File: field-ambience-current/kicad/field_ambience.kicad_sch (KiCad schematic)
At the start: 0 parts

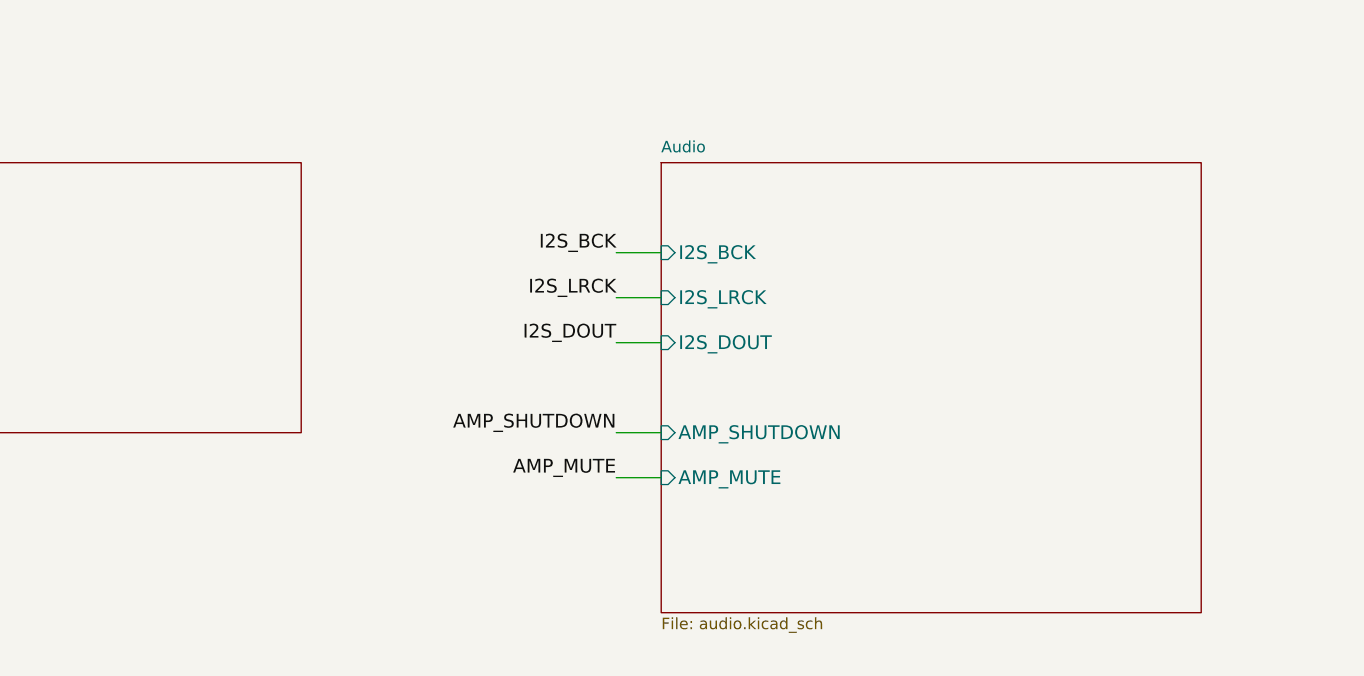
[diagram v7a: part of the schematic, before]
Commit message: v0.6.3-r5 N1-Fix: PCM5102A XSMT via MCP23017 GPA5 GPIO control
User-Wunsch: "lieber direkt haben als nicht haben" — explizite GPIO-
gesteuerte Pop-Suppression für PCM5102A statt nur statischem Pull-Up.

Hardware-Änderungen:

audio.kicad_sch (PCM5102A Pin 17 XSMT):
- BEFORE: R_XSMT 10k pull-up zu DVDD (chip statisch un-muted)
- AFTER:
  - R_XSMT_PD 10k pull-down zu GND (boot-safe default LOW = muted)
  - hier-input PCM_XSMT (vom MCP23017 via I²C-Steuerung)
  → Während Pico-Reset/Boot: XSMT bleibt LOW (DAC stumm), egal was
     der PCM5102A intern macht.

mcp.kicad_sch (MCP23017 GPA5 = Pin 26):
- BEFORE: NC_GPA5 reserve label (Pin ungenutzt)
- AFTER: hier-output PCM_XSMT (drives PCM5102A XSMT via PCM_XSMT net)

root.kicad_sch:
- MCP-Sheet-Box bekommt PCM_XSMT output pin (right side y=215)
- Audio-Sheet-Box bekommt PCM_XSMT input pin (left side y=240)
- Audio-Sheet-Box-Höhe von 50 → 55 erweitert (für zusätzlichen Pin)
- Cross-Sheet Label-Bridge PCM_XSMT zwischen MCP und Audio

Firmware-Sequenz (dokumentiert in SPEC v0.6.3-r5):
1. Boot: MCP23017-Pins default Input → R_XSMT_PD zieht XSMT LOW → PCM stumm
2. I²C-Init: MCP23017 GPA5 als Output, default 0 (XSMT bleibt LOW)
3. Power-Rails stabilisieren (~50 ms)
4. PAM8403 enable: GP28 (MUTE) HIGH, 100 ms später GP27 (SHDN) HIGH
5. PCM un-mute: MCP GPA5 HIGH → PCM_XSMT = +3V3 → DAC un-muted
6. → kein Pop am Speaker, kein DAC-Hochfahr-Knack

SPEC §7 MCP23017 Pin-Tabelle aktualisiert: GPA5 dokumentiert als
PCM_XSMT-Control, nicht mehr als reserve.

Analyzer-Status: 0 functional errors, 18 warnings (one less than r4 weil
NC_GPA5 label weg ist), 90 components (R_XSMT durch R_XSMT_PD ersetzt,
keine net-Change), 119 nets.

Verified via analyzer pin_nets:
- U3 Pin 17 (XSMT) → PCM_XSMT ✓
- U2 Pin 26 (GPA5) → PCM_XSMT ✓
- R_XSMT_PD pin1 = PCM_XSMT, pin2 = GND ✓

Damit ist Pop-Suppression jetzt belt-and-suspenders:
- Boot: PAM /MUTE LOW (R_MUTE_PD) + /SHDN LOW (R_SHDN_PD) + PCM XSMT LOW
- Operation: alle drei HIGH durch Firmware
- Shutd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
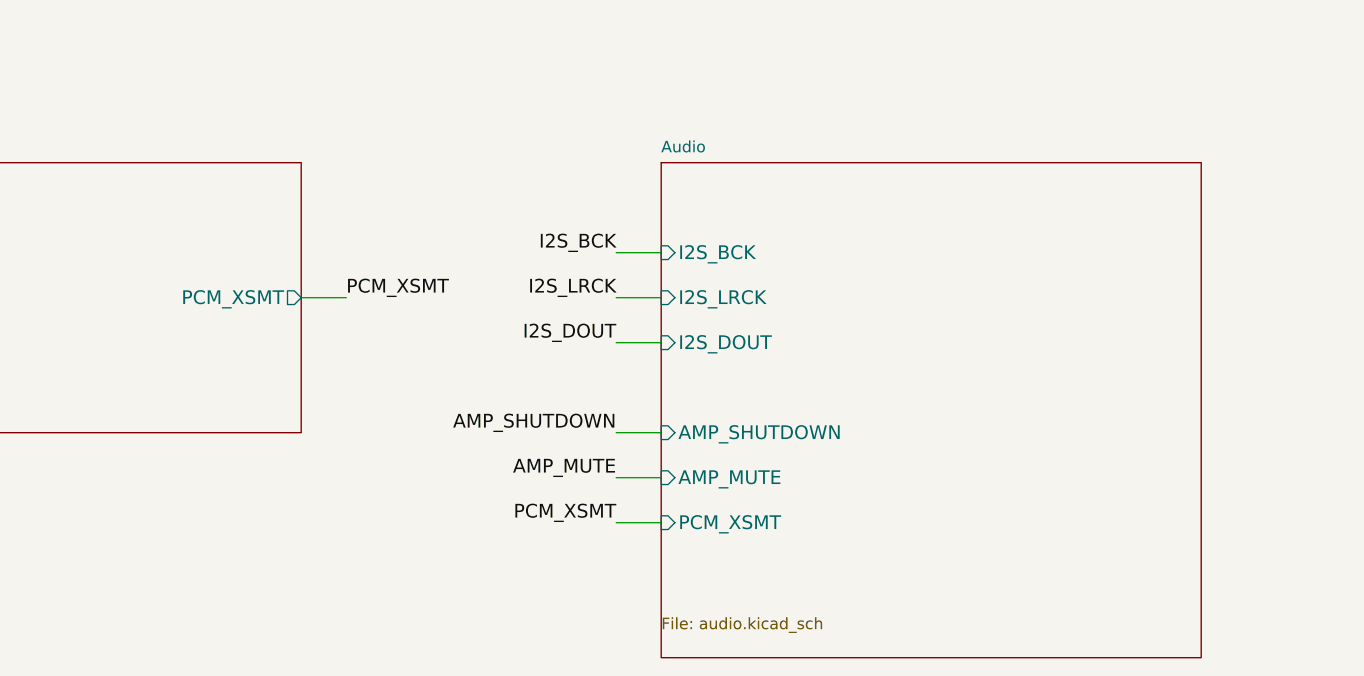
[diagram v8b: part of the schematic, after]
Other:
- sheet Audio ports: added PCM_XSMT; removed none
- sheet MCP23017 ports: added PCM_XSMT; removed none
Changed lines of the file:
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@@
     (pin "MCP_INT" output (at 130 220 180)
       (effects (font (size 1.524 1.524)) (justify left))
+)
+    (pin "PCM_XSMT" output (at 190 215 0)
+      (effects (font (size 1.524 1.524)) (justify right))
 ))
   (sheet (at 230 105) (size 60 70) (fields_autoplaced)
@@
   (wire (pts (xy 325 75) (xy 330 75)) (stroke (width 0) (type default)))
   (label "I2S_DOUT" (at 325 75 0) (effects (font (size 1.524 1.524)) (justify right bottom)))
-  (sheet (at 230 200) (size 60 50) (fields_autoplaced)
+  (sheet (at 230 200) (size 60 55) (fields_autoplaced)
     (stroke (width 0.1524) (type solid))
     (fill (color 0 0 0 0.0000))
@@
     (pin "AMP_MUTE" input (at 230 235 180)
       (effects (font (size 1.524 1.524)) (justify left))
+)
+    (pin "PCM_XSMT" input (at 230 240 180)
+      (effects (font (size 1.524 1.524)) (justify left))
 ))
   (wire (pts (xy 125 95) (xy 130 95)) (stroke (width 0) (type default)))
@@
   (wire (pts (xy 225 235) (xy 230 235)) (stroke (width 0) (type default)))
   (label "AMP_MUTE" (at 225 235 0) (effects (font (size 1.524 1.524)) (justify right bottom)))
+  (wire (pts (xy 190 215) (xy 195 215)) (stroke (width 0) (type default)))
+  (label "PCM_XSMT" (at 195 215 0) (effects (font (size 1.524 1.524)) (justify left bottom)))
+  (wire (pts (xy 225 240) (xy 230 240)) (stroke (width 0) (type default)))
+  (label "PCM_XSMT" (at 225 240 0) (effects (font (size 1.524 1.524)) (justify right bottom)))
   (wire (pts (xy 225 210) (xy 230 210)) (stroke (width 0) (type default)))
   (label "I2S_BCK" (at 225 210 0) (effects (font (size 1.524 1.524)) (justify right bottom)))
